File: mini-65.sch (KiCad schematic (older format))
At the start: 173 parts

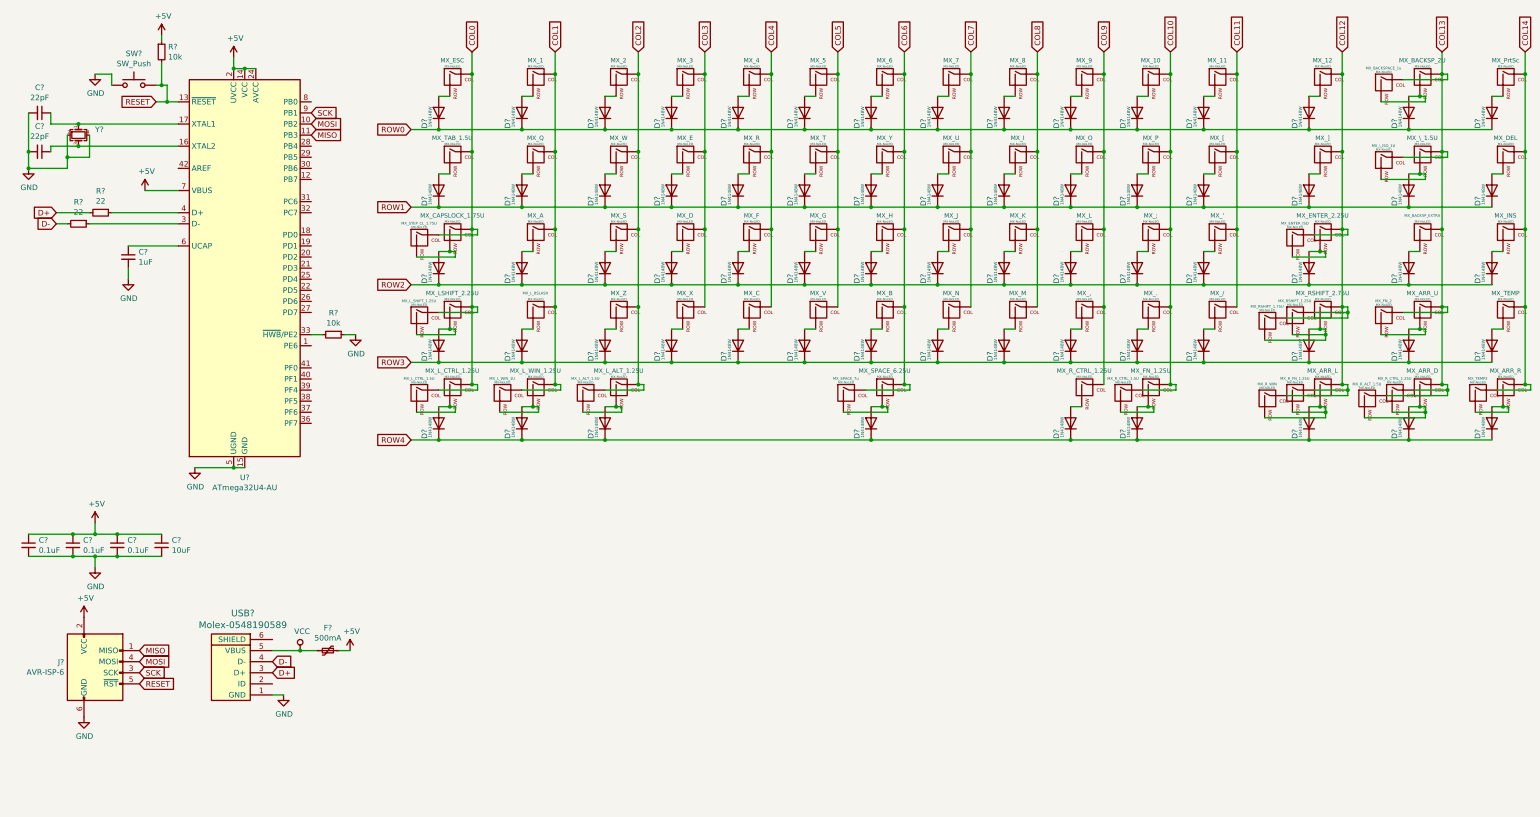
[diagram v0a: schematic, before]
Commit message: Annotated all components
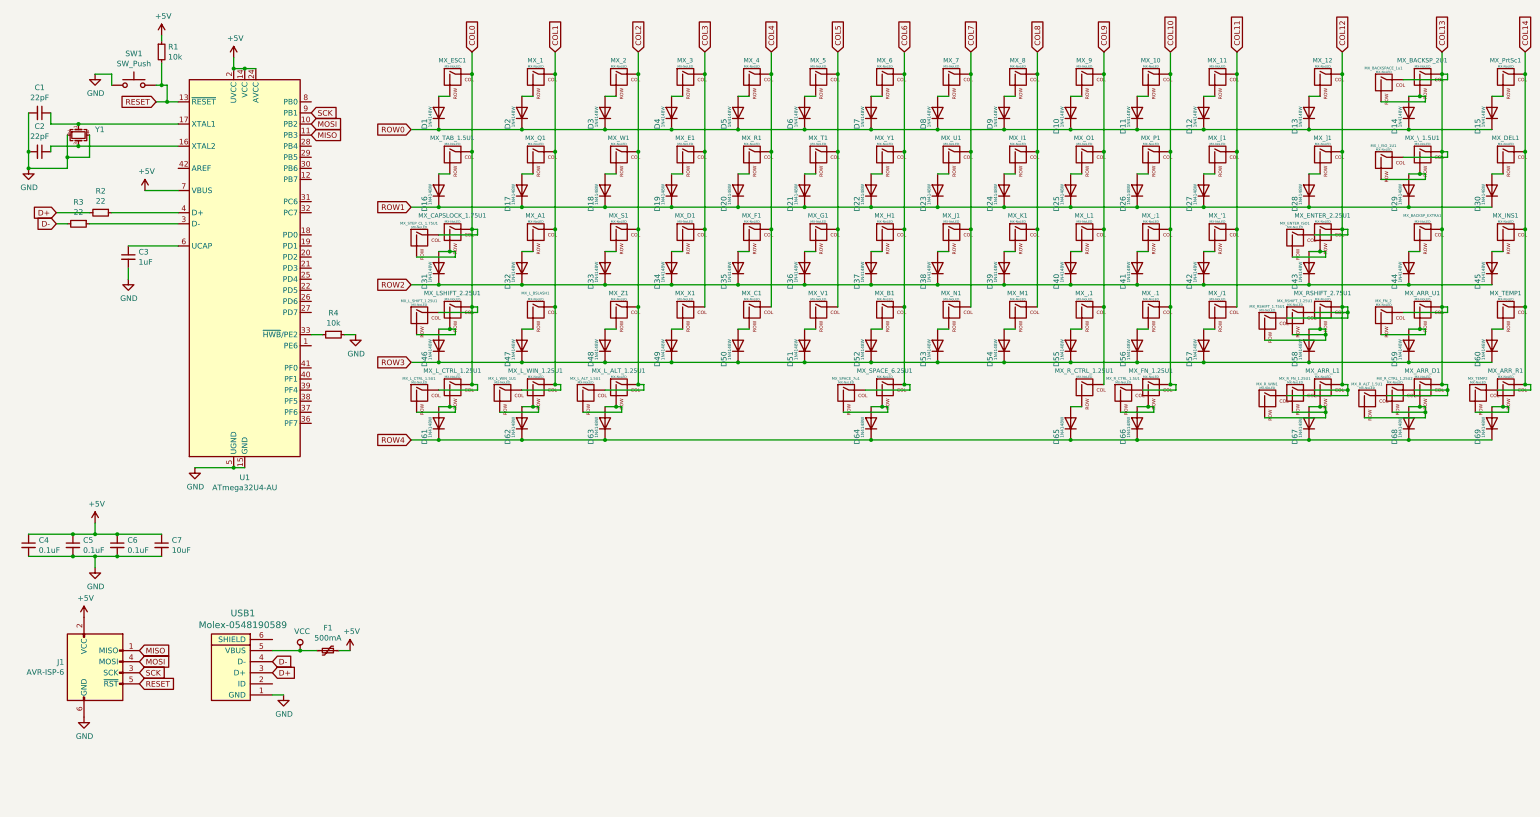
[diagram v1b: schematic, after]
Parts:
- gave numbers to parts that had none: 86
- renumbered MX_' to MX_'1, MX_, to MX_,1, MX_. to MX_.1, MX_/ to MX_/1, MX_; to MX_;1, MX_A to MX_A1, MX_ARR_D to MX_ARR_D1, MX_ARR_L to MX_ARR_L1, MX_ARR_R to MX_ARR_R1, MX_ARR_U to MX_ARR_U1, MX_B to MX_B1, MX_BACKSPACE_1u to MX_BACKSPACE_1u1, MX_BACKSP_2U to MX_BACKSP_2U1, MX_BACKSP_EXTRA to MX_BACKSP_EXTRA1, MX_C to MX_C1, MX_CAPSLOCK_1.75U to MX_CAPSLOCK_1.75U1, MX_D to MX_D1, MX_DEL to MX_DEL1, MX_E to MX_E1, MX_ENTER_2.25U to MX_ENTER_2.25U1, MX_ENTER_ISO to MX_ENTER_ISO1, MX_ESC to MX_ESC1, MX_F to MX_F1, MX_FN_1.25U to MX_FN_1.25U1, MX_G to MX_G1, MX_H to MX_H1, MX_I to MX_I1, MX_INS to MX_INS1, MX_J to MX_J1, MX_K to MX_K1, MX_L to MX_L1, MX_LSHIFT_2.25U to MX_LSHIFT_2.25U1, MX_L_ALT_1.25U to MX_L_ALT_1.25U1, MX_L_ALT_1.5U to MX_L_ALT_1.5U1, MX_L_BSLASH to MX_L_BSLASH1, MX_L_CTRL_1.25U to MX_L_CTRL_1.25U1, MX_L_CTRL_1.5U to MX_L_CTRL_1.5U1, MX_L_SHIFT_1.25U to MX_L_SHIFT_1.25U1, MX_L_WIN_1.25U to MX_L_WIN_1.25U1, MX_L_WIN_1U to MX_L_WIN_1U1, MX_M to MX_M1, MX_N to MX_N1, MX_O to MX_O1, MX_P to MX_P1, MX_PrtSc to MX_PrtSc1, MX_Q to MX_Q1, MX_R to MX_R1, MX_RSHIFT_1.25U to MX_RSHIFT_1.25U1, MX_RSHIFT_1.75U to MX_RSHIFT_1.75U1, MX_RSHIFT_2.75U to MX_RSHIFT_2.75U1, MX_R_ALT_1.5U to MX_R_ALT_1.5U1, MX_R_CTRL_1.25U to MX_R_CTRL_1.25U1, MX_R_CTRL_1.25U to MX_R_CTRL_1.25U2, MX_R_CTRL_1.5U to MX_R_CTRL_1.5U1, MX_R_FN_1.25U to MX_R_FN_1.25U1, MX_R_WIN to MX_R_WIN1, MX_S to MX_S1, MX_SPACE_6.25U to MX_SPACE_6.25U1, MX_SPACE_7u to MX_SPACE_7u1, MX_STEP_CL_1.75U to MX_STEP_CL_1.75U1, MX_T to MX_T1, MX_TAB_1.5U to MX_TAB_1.5U1, MX_TEMP to MX_TEMP1, MX_U to MX_U1, MX_V to MX_V1, MX_W to MX_W1, MX_X to MX_X1, MX_Y to MX_Y1, MX_Z to MX_Z1, MX_[ to MX_[1, MX_\_1.5U to MX_\_1.5U1, MX_\_ISO_1U to MX_\_ISO_1U1, MX_] to MX_]1

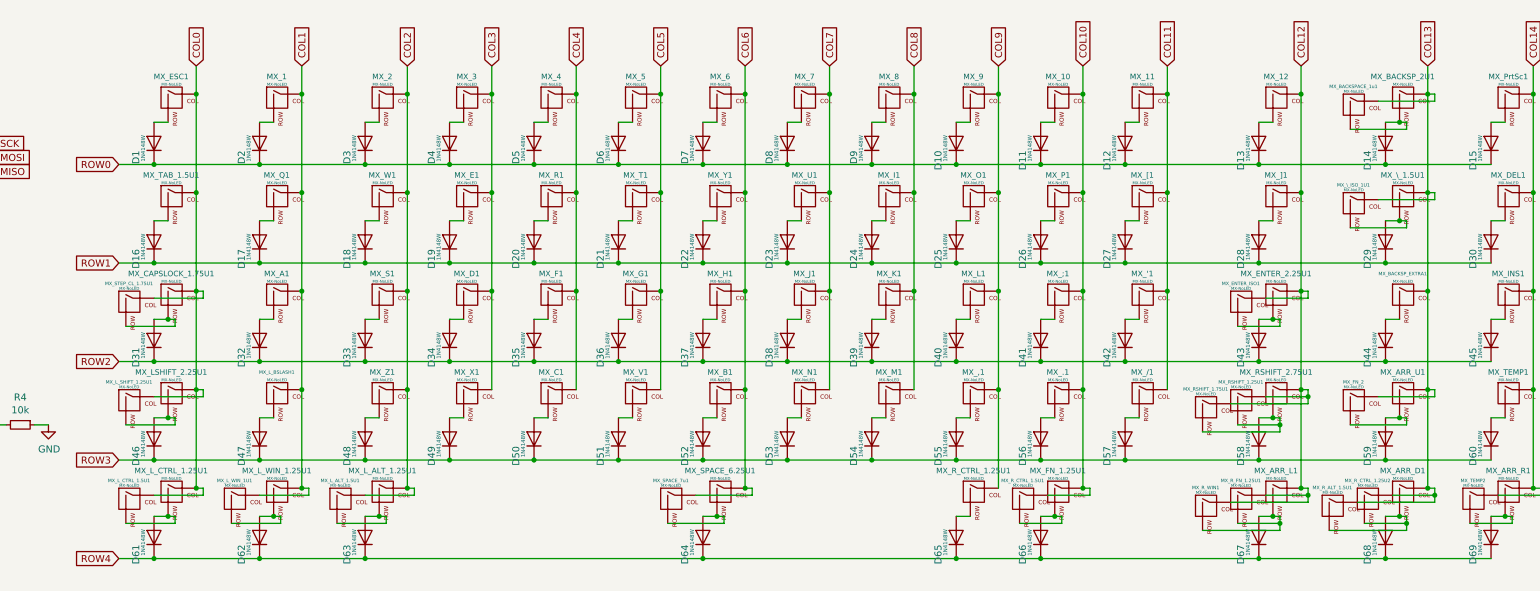
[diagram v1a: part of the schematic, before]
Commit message: Applied some footprints, adjusted MX names.
To make it easier to assign footprints, I added the U measurement to each key in the beginning of the name (MX_xU_KeyName).
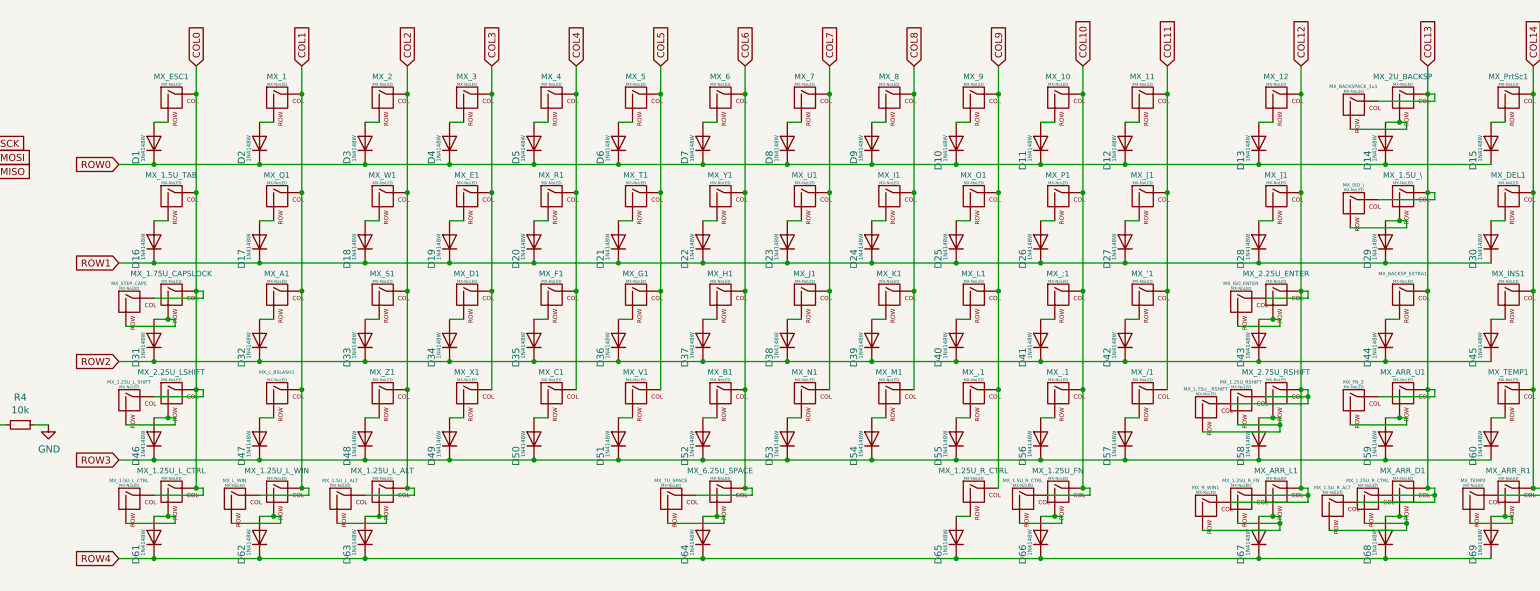
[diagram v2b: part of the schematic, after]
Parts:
- C1, C2, C3, C4, C5, C6, C7: footprint (none) -> Capacitor_SMD:C_0805_2012Metric
- D1, D10, D11, D12, D13, D14, D15, D16, D17, D18, D19, D2, D20, D21, D22, D23, D24, D25, D26, D27, D28, D29, D3, D30, D31, D32, D33, D34, D35, D36, D37, D38, D39, D4, D40, D41, D42, D43, D44, D45, D46, D47, D48, D49, D5, D50, D51, D52, D53, D54, D55, D56, D57, D58, D59, D6, D60, D61, D62, D63, D64, D65, D66, D67, D68, D69, D7, D8, D9: footprint Diode_SMD:D_SOD-123 -> canadian_footprints:D_SOD123_axial-dual
- F1: footprint (none) -> Fuse:Fuse_1206_3216Metric
- J1: footprint (none) -> Connector_PinHeader_2.54mm:PinHeader_2x03_P2.54mm_Vertical
- renumbered MX_FN_1.25U1 to MX_1.25U_FN, MX_L_ALT_1.25U1 to MX_1.25U_L_ALT, MX_L_CTRL_1.25U1 to MX_1.25U_L_CTRL, MX_L_SHIFT_1.25U1 to MX_1.25U_L_SHIFT, MX_L_WIN_1.25U1 to MX_1.25U_L_WIN, MX_RSHIFT_1.25U1 to MX_1.25U_RSHIFT, MX_R_CTRL_1.25U1 to MX_1.25U_R_CTRL, MX_R_CTRL_1.25U2 to MX_1.25U_R_CTRL, MX_R_FN_1.25U1 to MX_1.25U_R_FN, MX_L_ALT_1.5U1 to MX_1.5U_L_ALT, MX_L_CTRL_1.5U1 to MX_1.5U_L_CTRL, MX_R_ALT_1.5U1 to MX_1.5U_R_ALT, MX_R_CTRL_1.5U1 to MX_1.5U_R_CTRL, MX_TAB_1.5U1 to MX_1.5U_TAB, MX_\_1.5U1 to MX_1.5U_\, MX_CAPSLOCK_1.75U1 to MX_1.75U_CAPSLOCK, MX_RSHIFT_1.75U1 to MX_1.75U__RSHIFT, MX_ENTER_2.25U1 to MX_2.25U_ENTER, MX_LSHIFT_2.25U1 to MX_2.25U_LSHIFT, MX_RSHIFT_2.75U1 to MX_2.75U_RSHIFT, MX_BACKSP_2U1 to MX_2U_BACKSP, MX_SPACE_6.25U1 to MX_6.25U_SPACE, MX_SPACE_7u1 to MX_7U_SPACE, MX_ENTER_ISO1 to MX_ISO_ENTER, MX_\_ISO_1U1 to MX_ISO_\, MX_L_WIN_1U1 to MX_L_WIN, MX_STEP_CL_1.75U1 to MX_STEP_CAPS

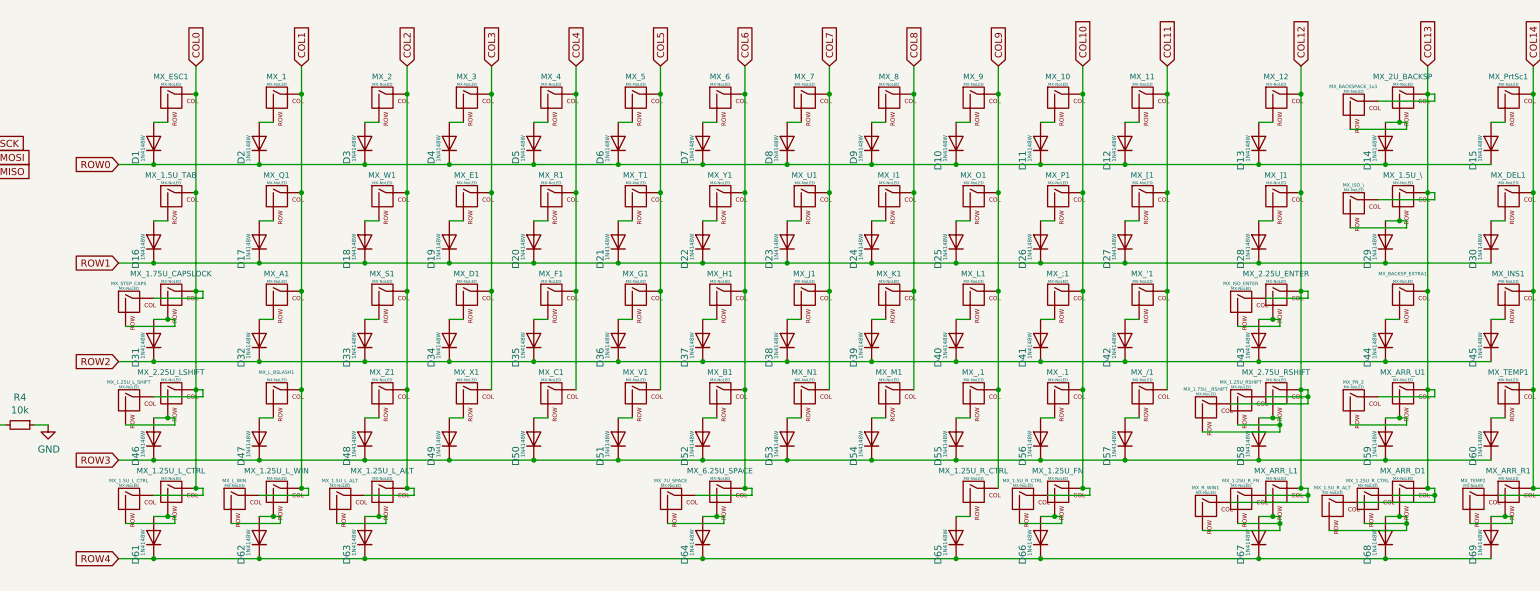
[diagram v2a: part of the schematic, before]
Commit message: Assigned the last of the footprints
Step before starting on the PCB. All footprints have been added.
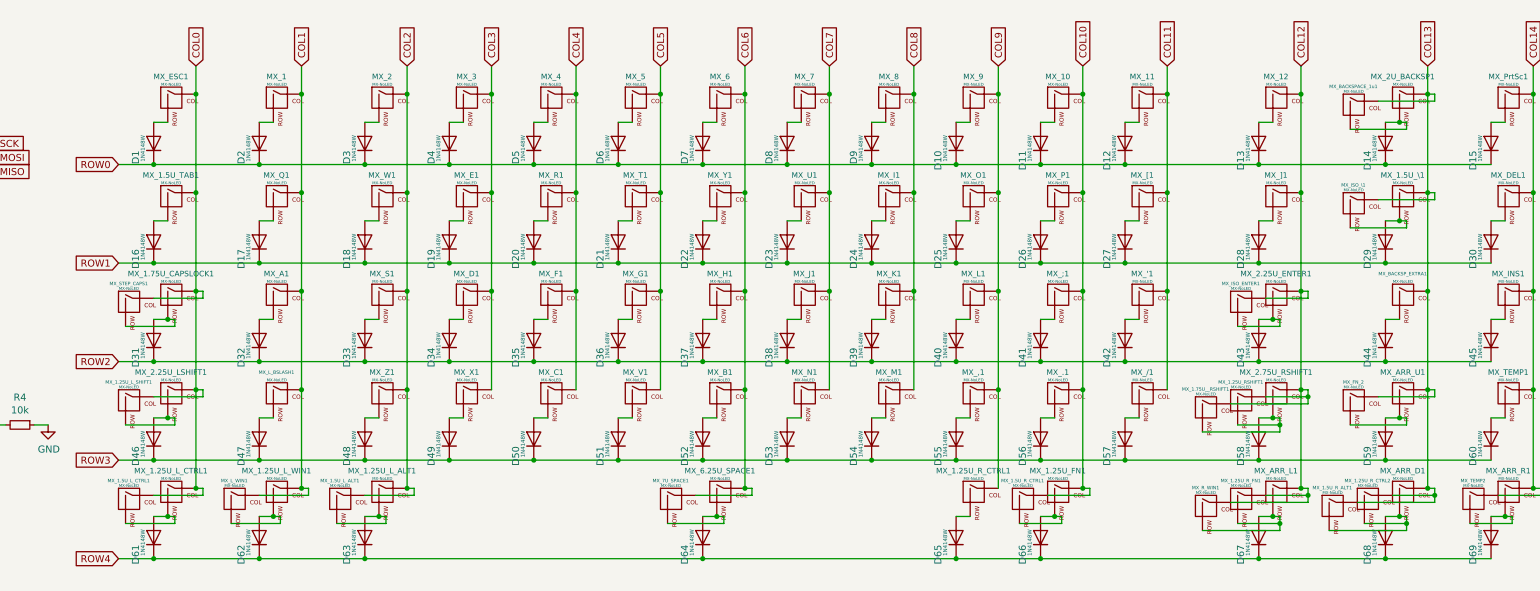
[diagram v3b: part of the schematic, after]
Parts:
- MX_'1, MX_,1, MX_.1, MX_/1, MX_1, MX_10, MX_11, MX_12, MX_2, MX_3, MX_4, MX_5, MX_6, MX_7, MX_8, MX_9, MX_;1, MX_A1, MX_ARR_D1, MX_ARR_L1, MX_ARR_R1, MX_ARR_U1, MX_B1, MX_BACKSPACE_1u1, MX_BACKSP_EXTRA1, MX_C1, MX_D1, MX_DEL1, MX_E1, MX_ESC1, MX_F1, MX_FN_2, MX_G1, MX_H1, MX_I1, MX_INS1, MX_J1, MX_K1, MX_L1, MX_L_BSLASH1, MX_M1, MX_N1, MX_O1, MX_P1, MX_PrtSc1, MX_Q1, MX_R1, MX_R_WIN1, MX_S1, MX_T1, MX_TEMP1, MX_TEMP2, MX_U1, MX_V1, MX_W1, MX_X1, MX_Y1, MX_Z1, MX_[1, MX_]1: footprint (none) -> MX_Alps_Hybrid:MX-1U-NoLED
- MX_1.25U_FN1: renamed from MX_1.25U_FN; footprint (none) -> MX_Alps_Hybrid:MX-1.25U-NoLED
- MX_1.25U_L_ALT1: renamed from MX_1.25U_L_ALT; footprint (none) -> MX_Alps_Hybrid:MX-1.25U-NoLED
- MX_1.25U_L_CTRL1: renamed from MX_1.25U_L_CTRL; footprint (none) -> MX_Alps_Hybrid:MX-1.25U-NoLED
- MX_1.25U_L_SHIFT1: renamed from MX_1.25U_L_SHIFT; footprint (none) -> MX_Alps_Hybrid:MX-1.25U-NoLED
- MX_1.25U_L_WIN1: renamed from MX_1.25U_L_WIN; footprint (none) -> MX_Alps_Hybrid:MX-1.25U-NoLED
- MX_1.25U_RSHIFT1: renamed from MX_1.25U_RSHIFT; footprint (none) -> MX_Alps_Hybrid:MX-1.25U-NoLED
- MX_1.25U_R_CTRL1, MX_1.25U_R_CTRL2: renamed from MX_1.25U_R_CTRL; footprint (none) -> MX_Alps_Hybrid:MX-1.25U-NoLED
- MX_1.25U_R_FN1: renamed from MX_1.25U_R_FN; footprint (none) -> MX_Alps_Hybrid:MX-1.25U-NoLED
- MX_1.5U_L_ALT1: renamed from MX_1.5U_L_ALT; footprint (none) -> MX_Alps_Hybrid:MX-1.5U-NoLED
- MX_1.5U_L_CTRL1: renamed from MX_1.5U_L_CTRL; footprint (none) -> MX_Alps_Hybrid:MX-1.5U-NoLED
- MX_1.5U_R_ALT1: renamed from MX_1.5U_R_ALT; footprint (none) -> MX_Alps_Hybrid:MX-1.5U-NoLED
- MX_1.5U_R_CTRL1: renamed from MX_1.5U_R_CTRL; footprint (none) -> MX_Alps_Hybrid:MX-1.5U-NoLED
- MX_1.5U_TAB1: renamed from MX_1.5U_TAB; footprint (none) -> MX_Alps_Hybrid:MX-1.5U-NoLED
- MX_1.5U_\1: renamed from MX_1.5U_\; footprint (none) -> MX_Alps_Hybrid:MX-1.5U-NoLED
- MX_1.75U_CAPSLOCK1: renamed from MX_1.75U_CAPSLOCK; footprint (none) -> MX_Alps_Hybrid:MX-1.75U-NoLED
- MX_1.75U__RSHIFT1: renamed from MX_1.75U__RSHIFT; footprint (none) -> MX_Alps_Hybrid:MX-1.75U-NoLED
- MX_2.25U_ENTER1: renamed from MX_2.25U_ENTER; footprint (none) -> MX_Alps_Hybrid:MX-2.25U-NoLED
- MX_2.25U_LSHIFT1: renamed from MX_2.25U_LSHIFT; footprint (none) -> MX_Alps_Hybrid:MX-2.25U-NoLED
- MX_2.75U_RSHIFT1: renamed from MX_2.75U_RSHIFT; footprint (none) -> MX_Alps_Hybrid:MX-2.75U-NoLED
- MX_2U_BACKSP1: renamed from MX_2U_BACKSP; footprint (none) -> MX_Alps_Hybrid:MX-2U-NoLED
- MX_6.25U_SPACE1: renamed from MX_6.25U_SPACE; footprint (none) -> MX_Alps_Hybrid:MX-6.25U-NoLED
- MX_7U_SPACE1: renamed from MX_7U_SPACE; footprint (none) -> MX_Alps_Hybrid:MX-7U-NoLED
- MX_ISO_ENTER1: renamed from MX_ISO_ENTER; footprint (none) -> MX_Alps_Hybrid:MX-ISO
- MX_ISO_\1: renamed from MX_ISO_\; footprint (none) -> MX_Alps_Hybrid:MX-1U-NoLED
- MX_L_WIN1: renamed from MX_L_WIN; footprint (none) -> MX_Alps_Hybrid:MX-1U-NoLED
- MX_STEP_CAPS1: renamed from MX_STEP_CAPS; footprint (none) -> MX_Alps_Hybrid:MX-1U-NoLED
- R1, R2, R3, R4: footprint (none) -> Resistor_SMD:R_0805_2012Metric
- SW1: footprint (none) -> random-keyboard-parts:SKQG-1155865
- USB1: footprint (none) -> random-keyboard-parts:Molex-0548190589
- Y1: footprint (none) -> Crystal:Crystal_SMD_3225-4Pin_3.2x2.5mm

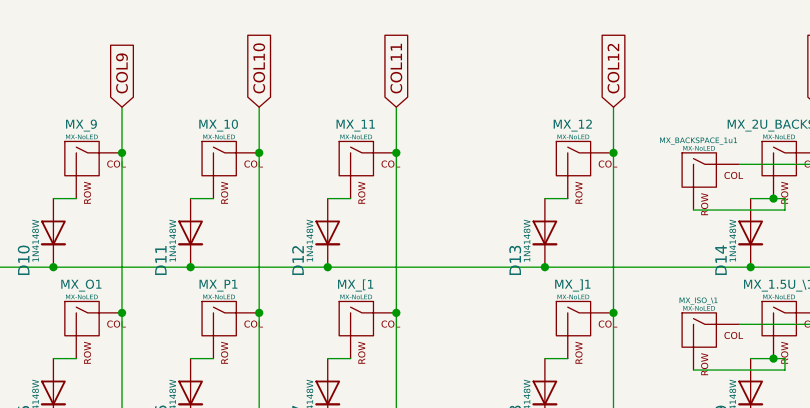
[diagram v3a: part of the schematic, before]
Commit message: Laid out keys on the PCB.
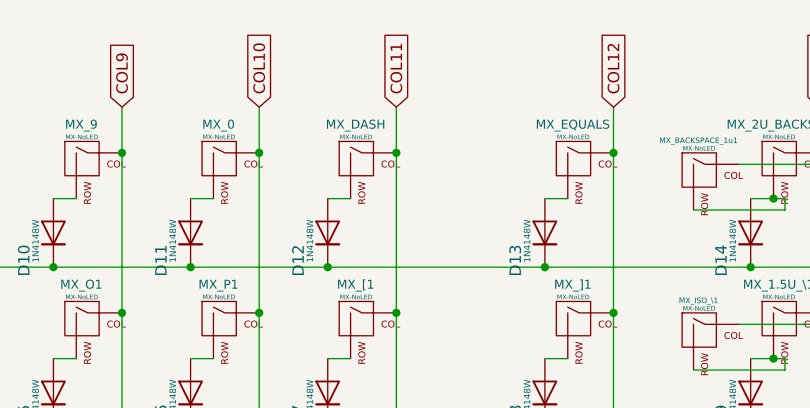
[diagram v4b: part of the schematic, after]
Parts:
- MX_ISO_ENTER1: footprint MX_Alps_Hybrid:MX-ISO -> MX_Only:MXOnly-ISO-ROTATED-ReversedStabilizers-NoLED
- renumbered MX_10 to MX_0, MX_11 to MX_DASH, MX_12 to MX_EQUALS
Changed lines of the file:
@@
 Wire Wire Line
 	11300 1300 11200 1300
-$Comp
-L MX_Alps_Hybrid:MX-NoLED MX_11
-U 1 1 5F45D4DD
-P 11350 1150
-F 0 "MX_11" H 11322 1324 39  0000 C CNN
-F 1 "MX-NoLED" H 11324 1269 20  0000 C CNN
-F 2 "MX_Alps_Hybrid:MX-1U-NoLED" H 10725 1125 60  0001 C CNN
-F 3 "" H 10725 1125 60  0001 C CNN
-	1    11350 1150
-	1    0    0    -1
-$EndComp
 Wire Wire Line
 	10700 1300 10600 1300
-$Comp
-L MX_Alps_Hybrid:MX-NoLED MX_10
-U 1 1 5F45D4E4
-P 10750 1150
-F 0 "MX_10" H 10722 1324 39  0000 C CNN
-F 1 "MX-NoLED" H 10724 1269 20  0000 C CNN
-F 2 "MX_Alps_Hybrid:MX-1U-NoLED" H 10125 1125 60  0001 C CNN
-F 3 "" H 10125 1125 60  0001 C CNN
-	1    10750 1150
-	1    0    0    -1
-$EndComp
 Wire Wire Line
 	10900 1100 10900 900
@@
 	12250 1300 12150 1300
 $Comp
-L MX_Alps_Hybrid:MX-NoLED MX_12
+L MX_Alps_Hybrid:MX-NoLED MX_EQUALS
 U 1 1 5F474929
 P 12300 1150
-F 0 "MX_12" H 12272 1324 39  0000 C CNN
+F 0 "MX_EQUALS" H 12272 1324 39  0000 C CNN
 F 1 "MX-NoLED" H 12274 1269 20  0000 C CNN
 F 2 "MX_Alps_Hybrid:MX-1U-NoLED" H 11675 1125 60  0001 C CNN
@@
 F 0 "MX_ISO_ENTER1" H 12022 2754 24  0000 C CNN
 F 1 "MX-NoLED" H 12024 2719 20  0000 C CNN
-F 2 "MX_Alps_Hybrid:MX-ISO" H 11425 2575 60  0001 C CNN
+F 2 "MX_Only:MXOnly-ISO-ROTATED-ReversedStabilizers-NoLED" H 11425 2575 60  0001 C CNN
 F 3 "" H 11425 2575 60  0001 C CNN
 	1    12050 2600
@@
 	1    0    0    -1
 $EndComp
+$Comp
+L MX_Alps_Hybrid:MX-NoLED MX_DASH
+U 1 1 5F45D4DD
+P 11350 1150
+F 0 "MX_DASH" H 11322 1324 39  0000 C CNN
+F 1 "MX-NoLED" H 11324 1269 20  0000 C CNN
+F 2 "MX_Alps_Hybrid:MX-1U-NoLED" H 10725 1125 60  0001 C CNN
+F 3 "" H 10725 1125 60  0001 C CNN
+	1    11350 1150
+	1    0    0    -1
+$EndComp
+$Comp
+L MX_Alps_Hybrid:MX-NoLED MX_0
+U 1 1 5F45D4E4
+P 10750 1150
+F 0 "MX_0" H 10722 1324 39  0000 C CNN
+F 1 "MX-NoLED" H 10724 1269 20  0000 C CNN
+F 2 "MX_Alps_Hybrid:MX-1U-NoLED" H 10125 1125 60  0001 C CNN
+F 3 "" H 10125 1125 60  0001 C CNN
+	1    10750 1150
+	1    0    0    -1
+$EndComp
